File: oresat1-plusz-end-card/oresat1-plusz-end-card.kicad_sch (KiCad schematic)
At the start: 39 parts, among them J1 J-SAMTEC-TFM-120-01-L-D-RA, J2 Harwin M55-7101242R, J3 Harwin M55-7101242R, J4 Harwin M55-7101242R, J5 Harwin M55-7101242R, J6 Conn_Coaxial

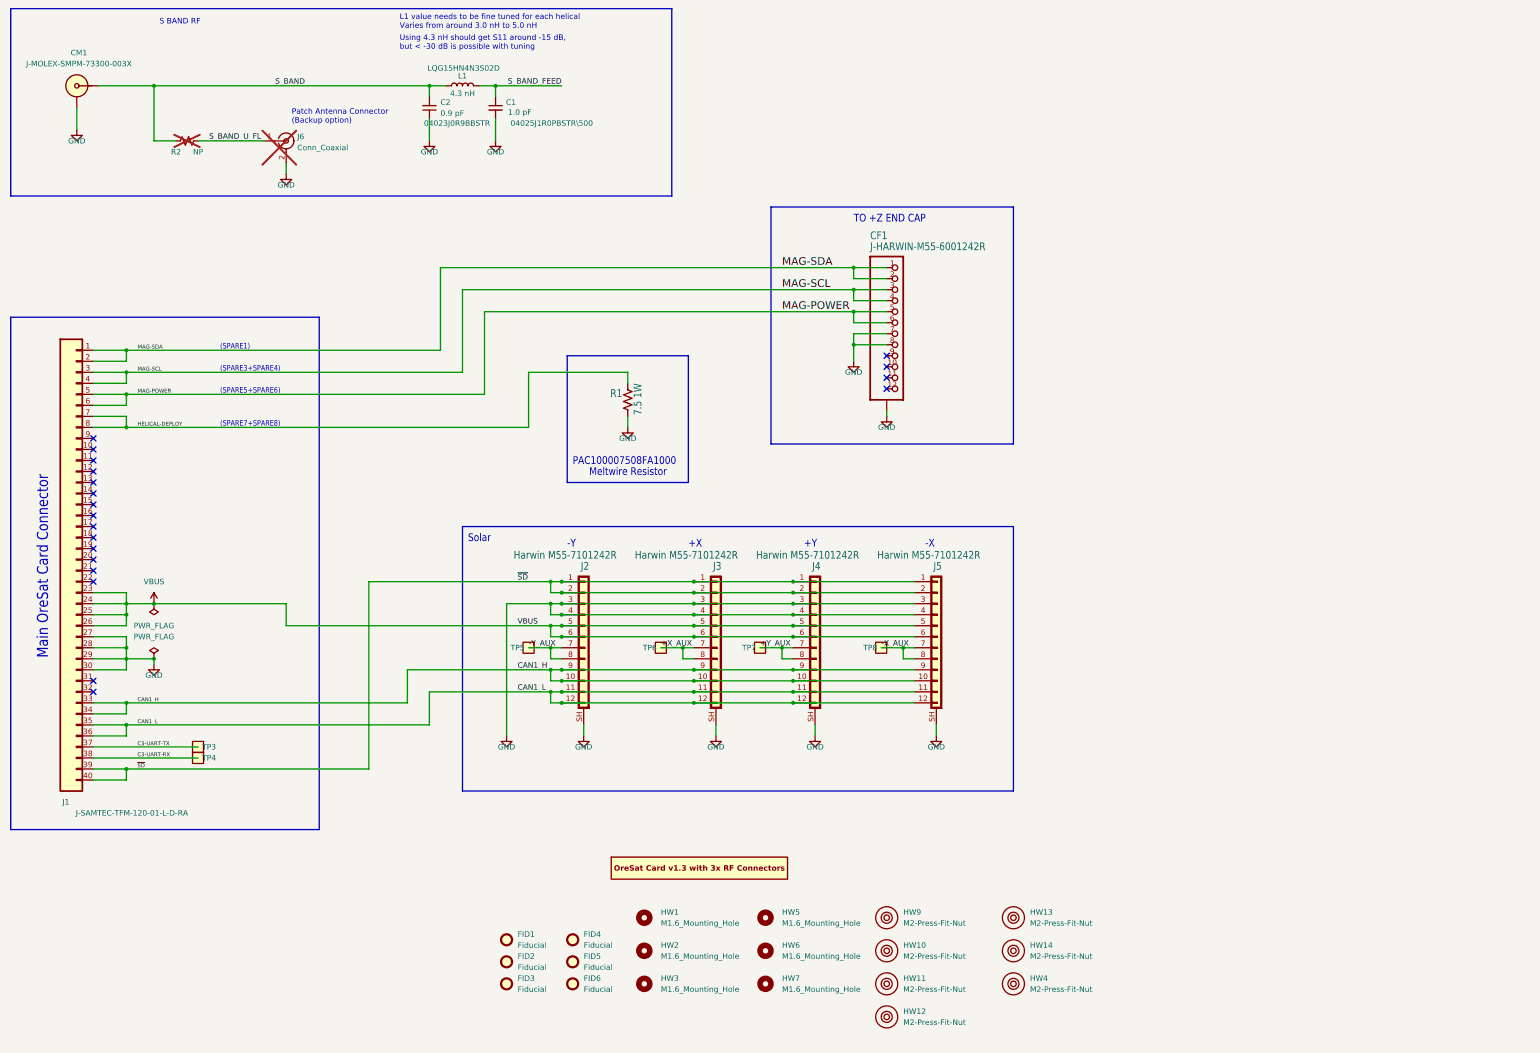
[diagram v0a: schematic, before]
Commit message: add OPD and deployer circuitry
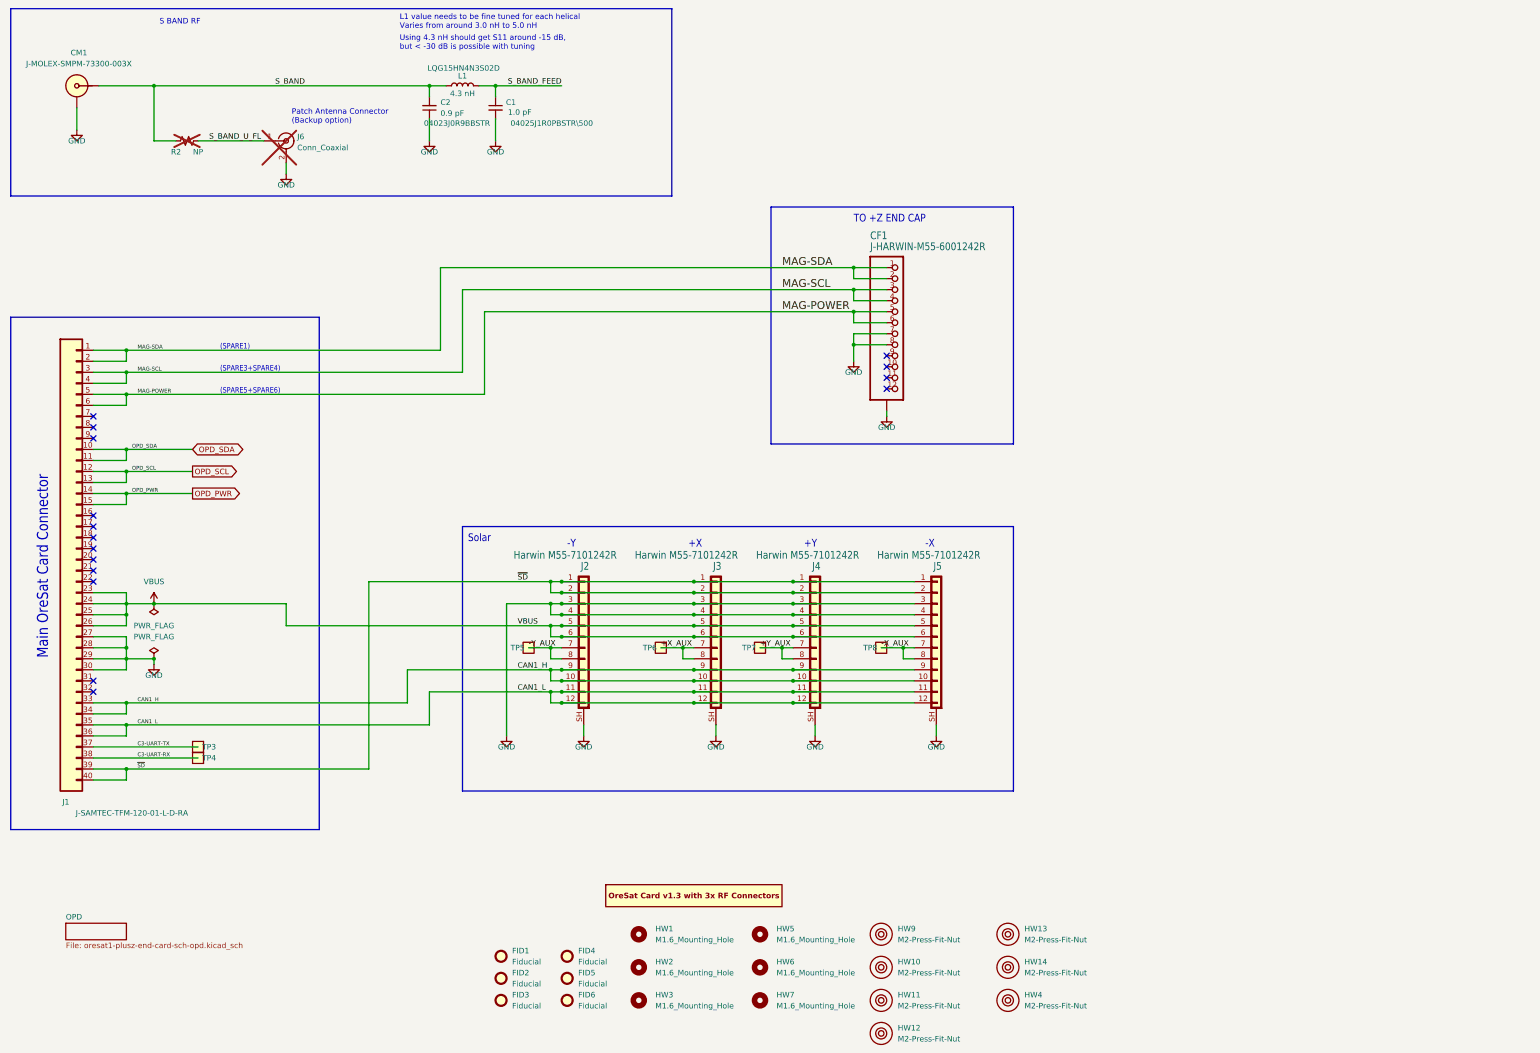
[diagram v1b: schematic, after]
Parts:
- removed R1: 7.5 1W, oresat-passives:R-PAC100-FOR-MELTWIRE, symbol Device:R_US
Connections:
- net OPD_SDA: now reaches J1.10
- net OPD_SDA: now also J1.11
- net OPD_SCL: now reaches J1.12
- net OPD_SCL: now also J1.13
- net OPD_PWR: now reaches J1.14
- net OPD_PWR: now also J1.15
- net HELICAL-DEPLOY: no longer names the net of J1.7
- net HELICAL-DEPLOY: no longer J1.8
- no-connect marks 20 -> 16
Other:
- added sheet OPD (oresat1-plusz-end-card-sch-opd.kicad_sch)
- note removed: "(SPARE7+SPARE8)"
- note removed: "Meltwire Resistor"
- note removed: "PAC100007508FA1000"
- moved on the sheet: FID1, FID2, FID3, FID4, FID5, FID6, HW1, HW10, HW11, HW12, HW13, HW14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

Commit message: v1.1, theoretically done
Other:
- company: (none) -> Portland State Aerospace Society
- title: +Z End Card w/ Turnstile -> OreSat1 +Z End Card
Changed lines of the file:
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@@
 	(paper "USLedger")
 	(title_block
-		(title "+Z End Card w/ Turnstile")
-		(date "2024-08-20")
-		(rev "1.4")
+		(title "OreSat1 +Z End Card")
+		(date "2026-02-18")
+		(rev "v1.1")
+		(company "Portland State Aerospace Society")
 	)
 	(text "TO +Z END CAP"

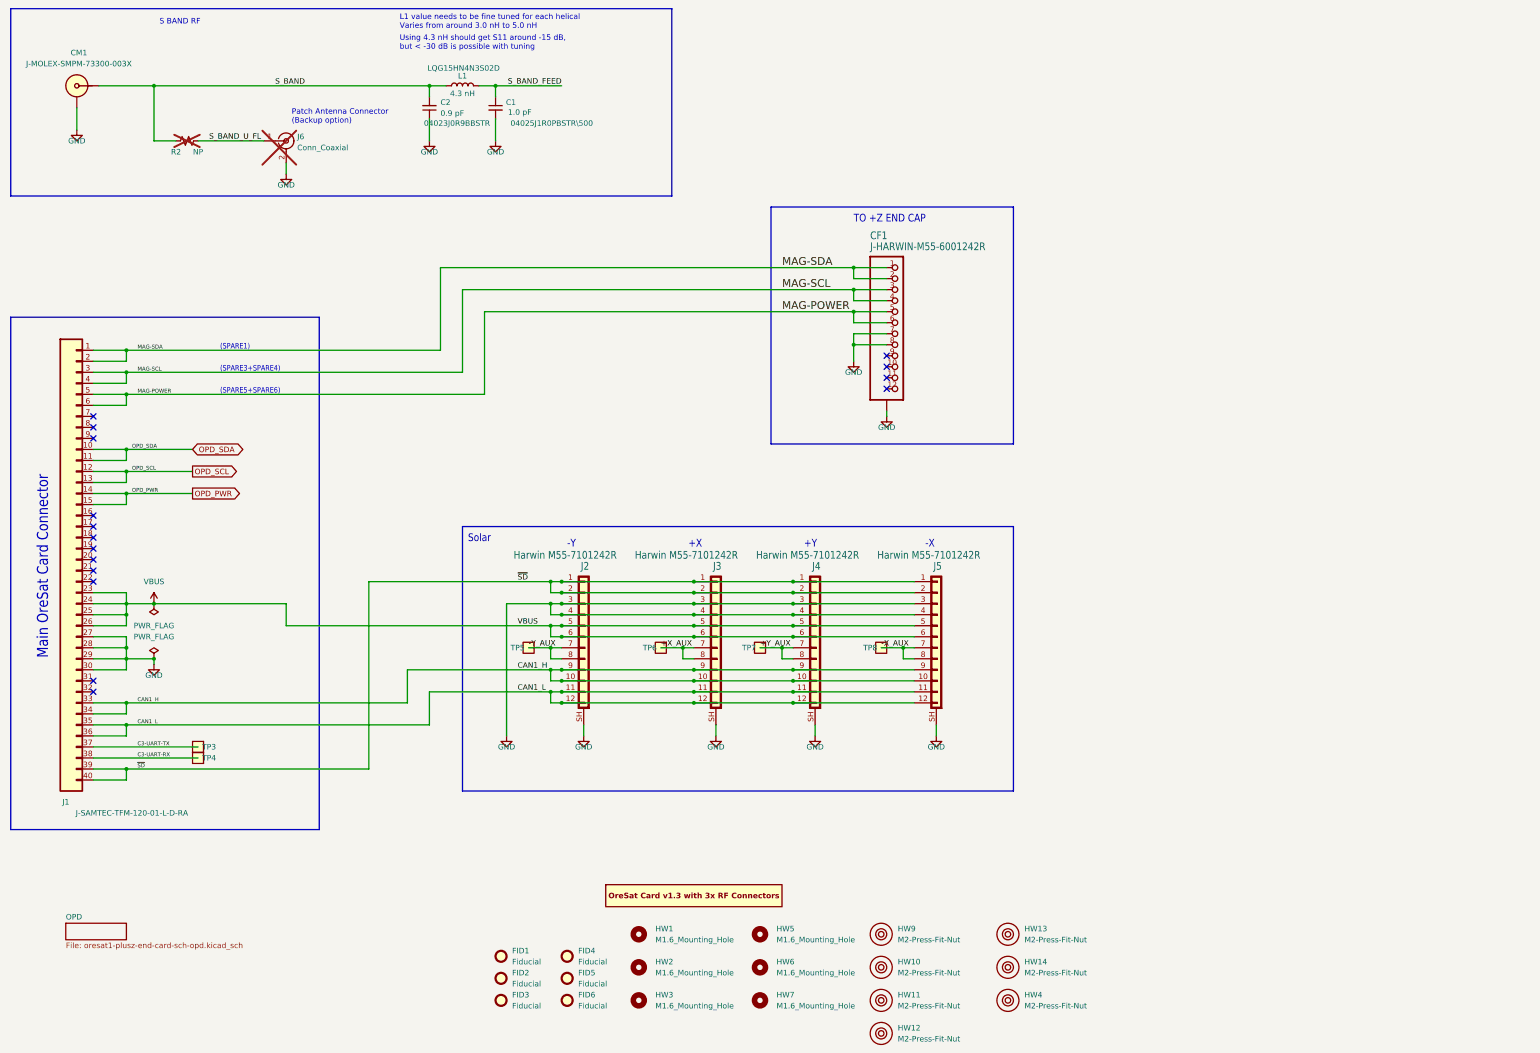
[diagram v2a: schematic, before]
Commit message: Changed symbols & fab layout
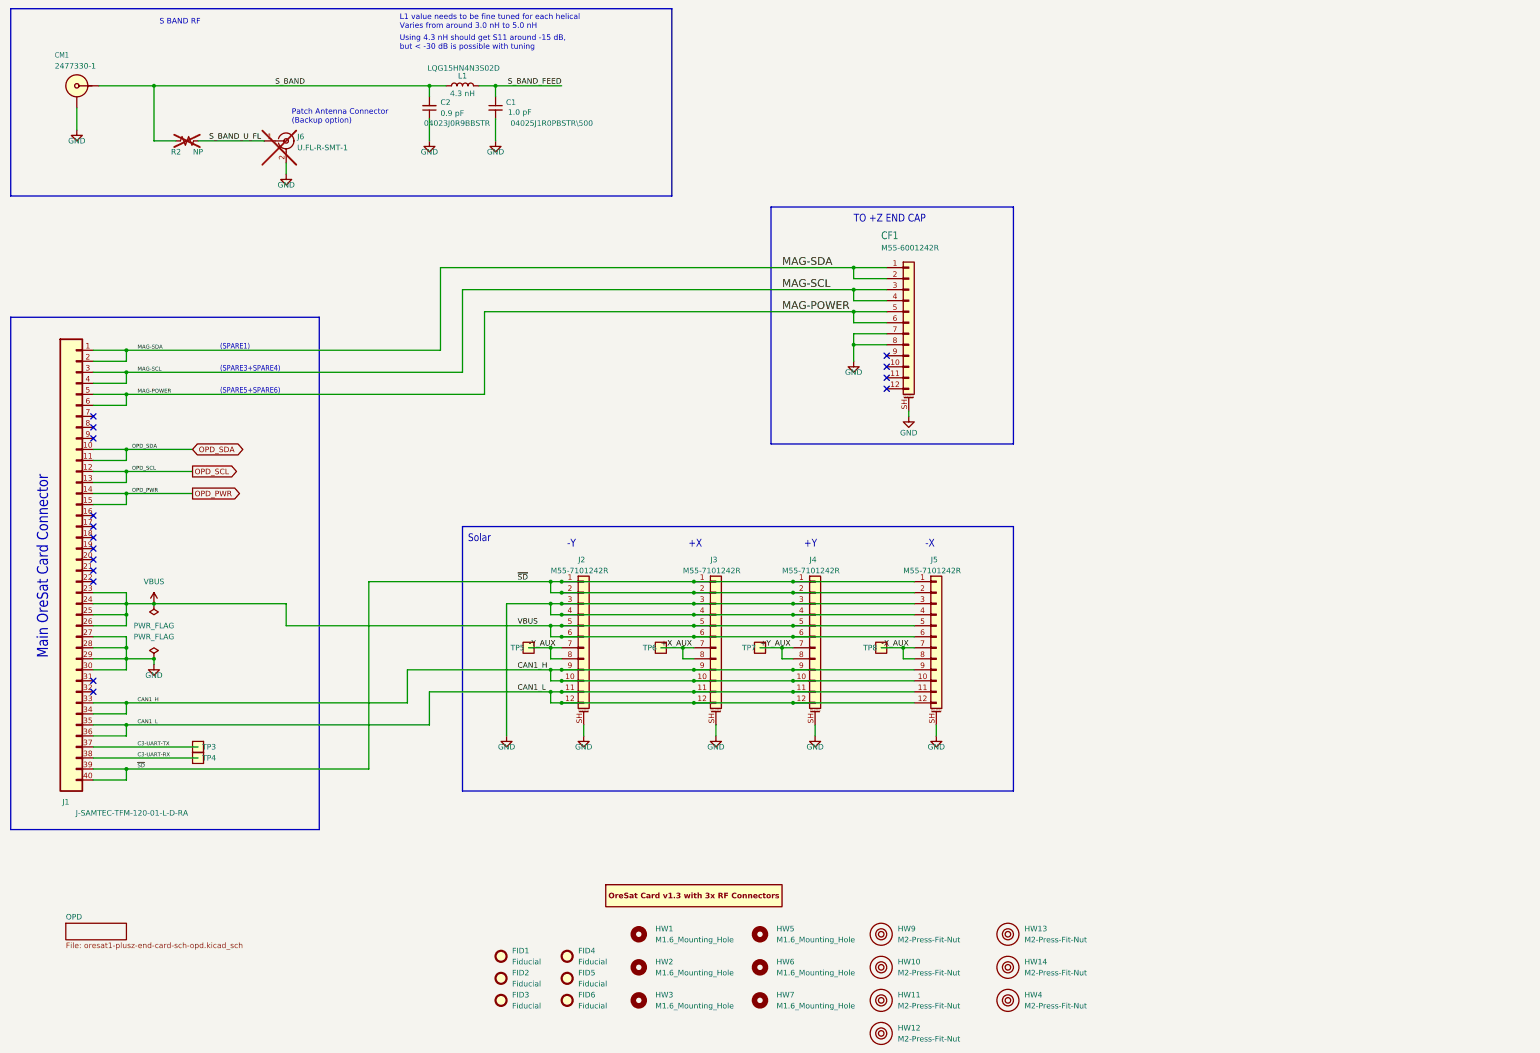
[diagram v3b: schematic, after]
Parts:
- removed CF1: J-HARWIN-M55-6001242R, oresat-connectors:J-Harwin-M55-60X1242R, symbol oresat-connectors:J-HARWIN-M55-6001242R
- removed J2, J3, J4, J5: Harwin M55-7101242R, oresat-connectors:J-Harwin-M55-7101242R, symbol oresat-connectors:Harwin M55-7101242R
- added CF1: M55-6001242R, oresat-connectors:J-Harwin-M55-60X1242R, symbol Connector_Generic_MountingPin:Conn_01x12_MountingPin
- added J2, J3, J4, J5: M55-7101242R, oresat-connectors:J-Harwin-M55-7101242R, symbol Connector_Generic_MountingPin:Conn_01x12_MountingPin
- C1, C2, J1, L1: DIST DigiKey -> (none)
- CM1: value J-MOLEX-SMPM-73300-003X -> 2477330-1; DIS (none) -> DigiKey; DIST DigiKey -> (none); DPN WM10772-ND -> 343-2477330-1CT-ND; MFR DigiKey -> TE Connectivity Linx; MPN 952-3851-1-ND -> 2477330-1
- J6: value Conn_Coaxial -> U.FL-R-SMT-1; DIS (none) -> DigiKey; DIST DigiKey -> (none); now in the parts list
- R2: DIST Digikey -> (none)
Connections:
- net +X_AUX: now also J3.7 (Pin_7), J3.8 (Pin_8)
- net +Y_AUX: now also J4.7 (Pin_7), J4.8 (Pin_8)
- net -X_AUX: now also J5.7 (Pin_7), J5.8 (Pin_8)
- net -Y_AUX: now also J2.7 (Pin_7), J2.8 (Pin_8)
- net CAN1_H: now also J2.10 (Pin_10), J2.9 (Pin_9), J3.10 (Pin_10), J3.9 (Pin_9), J4.10 (Pin_10), J4.9 (Pin_9), J5.10 (Pin_10), J5.9 (Pin_9)
- net CAN1_L: now also J2.11 (Pin_11), J2.12 (Pin_12), J3.11 (Pin_11), J3.12 (Pin_12), J4.11 (Pin_11), J4.12 (Pin_12), J5.11 (Pin_11), J5.12 (Pin_12)
- net GND: now also CF1.7 (Pin_7), CF1.8 (Pin_8), CF1.SH (MountPin), J2.3 (Pin_3), J2.4 (Pin_4), J2.SH (MountPin), J3.3 (Pin_3), J3.4 (Pin_4), J3.SH (MountPin), J4.3 (Pin_3), J4.4 (Pin_4), J4.SH (MountPin), J5.3 (Pin_3), J5.4 (Pin_4), J5.SH (MountPin)
- net MAG-POWER: now also CF1.5 (Pin_5), CF1.6 (Pin_6)
- net MAG-SCL: now also CF1.3 (Pin_3), CF1.4 (Pin_4)
- net MAG-SDA: now also CF1.1 (Pin_1), CF1.2 (Pin_2)
- net VBUS: now also J2.5 (Pin_5), J2.6 (Pin_6), J3.5 (Pin_5), J3.6 (Pin_6), J4.5 (Pin_5), J4.6 (Pin_6), J5.5 (Pin_5), J5.6 (Pin_6)
- net ~{SD}: now also J2.1 (Pin_1), J2.2 (Pin_2), J3.1 (Pin_1), J3.2 (Pin_2), J4.1 (Pin_1), J4.2 (Pin_2), J5.1 (Pin_1), J5.2 (Pin_2)

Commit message: Design review, more to do!
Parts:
- removed TP5, TP6, TP7: TestPoint-MinTH, oresat-misc:TestPoint-0.75mm-th, symbol oresat-misc:Test-Point-0.75mm-th
- FID1, FID2, FID3, FID4, FID5, FID6, PCB1: now left out of the parts list
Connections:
- net +X_AUX renamed PX-UART-RX
- net PX-UART-RX: no longer J3.7 (Pin_7)
- net +Y_AUX: no longer names the net of J4.7 (Pin_7)
- net +Y_AUX: no longer J4.8 (Pin_8)
- net -Y_AUX: no longer names the net of J2.7 (Pin_7)
- net -Y_AUX: no longer J2.8 (Pin_8)
- new net PX-UART-TX: J3.7 (Pin_7)
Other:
- note removed: "(SPARE1)"
- note removed: "(SPARE3+SPARE4)"
- note removed: "(SPARE5+SPARE6)"

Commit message: bom finished
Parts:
- C1, C2, J1, L1: DIS (none) -> DigiKey
- HW10, HW11, HW12, HW13, HW14, HW4, HW9, TP3, TP4, TP8: now left out of the parts list
